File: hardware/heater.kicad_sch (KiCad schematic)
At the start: 5 parts

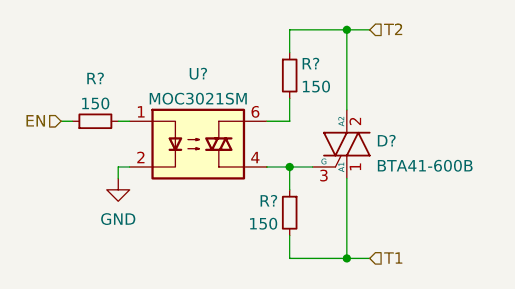
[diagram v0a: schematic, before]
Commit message: assigned footprints
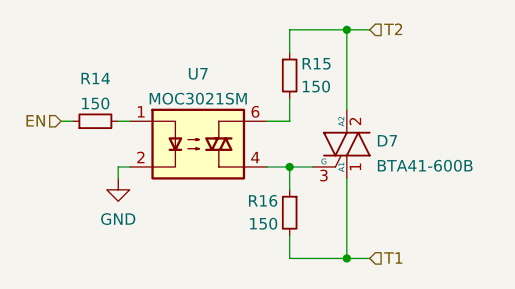
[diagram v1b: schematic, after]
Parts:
- D7: renamed from D?; footprint (none) -> Package_TO_SOT_THT:TO-3P-3_Horizontal_TabDown
- R14, R15, R16: renamed from R?; footprint (none) -> Resistor_SMD:R_0603_1608Metric
- gave numbers to parts that had none: 1
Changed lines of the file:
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@@
   (symbol (lib_id "Device:R_Small") (at 154.94 100.33 0)
     (in_bom yes) (on_board yes)
-    (property "Reference" "R?" (id 0) (at 156.21 99.06 0)
+    (property "Reference" "R15" (id 0) (at 156.21 99.06 0)
       (effects (font (size 1.27 1.27)) (justify left))
     )
@@
       (effects (font (size 1.27 1.27)) (justify left))
     )
-    (property "Footprint" "" (id 2) (at 154.94 100.33 0)
+    (property "Footprint" "Resistor_SMD:R_0603_1608Metric" (id 2) (at 154.94 100.33 0)
       (effects (font (size 1.27 1.27)) hide)
     )
@@
   (symbol (lib_id "power:GND") (at 135.89 111.76 0)
     (in_bom yes) (on_board yes) (fields_autoplaced)
-    (property "Reference" "#PWR?" (id 0) (at 135.89 118.11 0)
+    (property "Reference" "#PWR036" (id 0) (at 135.89 118.11 0)
       (effects (font (size 1.27 1.27)) hide)
     )
@@
   (symbol (lib_id "Isolator:TLP3021") (at 144.78 107.95 0)
     (in_bom yes) (on_board yes) (fields_autoplaced)
-    (property "Reference" "U?" (id 0) (at 144.78 100.1735 0))
+    (property "Reference" "U7" (id 0) (at 144.78 100.1735 0))
     (property "Value" "MOC3021SM" (id 1) (at 144.78 102.9486 0))
     (property "Footprint" "Package_DIP:SMDIP-6_W9.53mm_Clearance8mm" (id 2) (at 139.7 113.03 0)
@@
   (symbol (lib_id "Device:R_Small") (at 154.94 115.57 0) (mirror y)
     (in_bom yes) (on_board yes)
-    (property "Reference" "R?" (id 0) (at 153.67 114.3 0)
+    (property "Reference" "R16" (id 0) (at 153.67 114.3 0)
       (effects (font (size 1.27 1.27)) (justify left))
     )
@@
       (effects (font (size 1.27 1.27)) (justify left))
     )
-    (property "Footprint" "" (id 2) (at 154.94 115.57 0)
+    (property "Footprint" "Resistor_SMD:R_0603_1608Metric" (id 2) (at 154.94 115.57 0)
       (effects (font (size 1.27 1.27)) hide)
     )
@@
   (symbol (lib_id "Device:R_Small") (at 133.35 105.41 90)
     (in_bom yes) (on_board yes)
-    (property "Reference" "R?" (id 0) (at 133.35 100.7069 90))
+    (property "Reference" "R14" (id 0) (at 133.35 100.7069 90))
     (property "Value" "150" (id 1) (at 133.35 103.482 90))
-    (property "Footprint" "" (id 2) (at 133.35 105.41 0)
+    (property "Footprint" "Resistor_SMD:R_0603_1608Metric" (id 2) (at 133.35 105.41 0)
       (effects (font (size 1.27 1.27)) hide)
     )
@@
   (symbol (lib_id "Device:Q_TRIAC_A1A2G") (at 161.29 107.95 0)
     (in_bom yes) (on_board yes) (fields_autoplaced)
-    (property "Reference" "D?" (id 0) (at 164.5666 107.6257 0)
+    (property "Reference" "D7" (id 0) (at 164.5666 107.6257 0)
       (effects (font (size 1.27 1.27)) (justify left))
     )
@@
       (effects (font (size 1.27 1.27)) (justify left))
     )
-    (property "Footprint" "" (id 2) (at 163.195 107.315 90)
+    (property "Footprint" "Package_TO_SOT_THT:TO-3P-3_Horizontal_TabDown" (id 2) (at 163.195 107.315 90)
       (effects (font (size 1.27 1.27)) hide)
     )

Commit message: layout WIP
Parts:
- renumbered D7 to D6, R14 to R11, R15 to R12, R16 to R13, U7 to U6
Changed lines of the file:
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@@
   (symbol (lib_id "Device:R_Small") (at 154.94 100.33 0)
     (in_bom yes) (on_board yes)
-    (property "Reference" "R15" (id 0) (at 156.21 99.06 0)
+    (property "Reference" "R12" (id 0) (at 156.21 99.06 0)
       (effects (font (size 1.27 1.27)) (justify left))
     )
@@
   (symbol (lib_id "Isolator:TLP3021") (at 144.78 107.95 0)
     (in_bom yes) (on_board yes) (fields_autoplaced)
-    (property "Reference" "U7" (id 0) (at 144.78 100.1735 0))
+    (property "Reference" "U6" (id 0) (at 144.78 100.1735 0))
     (property "Value" "MOC3021SM" (id 1) (at 144.78 102.9486 0))
     (property "Footprint" "Package_DIP:SMDIP-6_W9.53mm_Clearance8mm" (id 2) (at 139.7 113.03 0)
@@
   (symbol (lib_id "Device:R_Small") (at 154.94 115.57 0) (mirror y)
     (in_bom yes) (on_board yes)
-    (property "Reference" "R16" (id 0) (at 153.67 114.3 0)
+    (property "Reference" "R13" (id 0) (at 153.67 114.3 0)
       (effects (font (size 1.27 1.27)) (justify left))
     )
@@
   (symbol (lib_id "Device:R_Small") (at 133.35 105.41 90)
     (in_bom yes) (on_board yes)
-    (property "Reference" "R14" (id 0) (at 133.35 100.7069 90))
+    (property "Reference" "R11" (id 0) (at 133.35 100.7069 90))
     (property "Value" "150" (id 1) (at 133.35 103.482 90))
     (property "Footprint" "Resistor_SMD:R_0603_1608Metric" (id 2) (at 133.35 105.41 0)
@@
   (symbol (lib_id "Device:Q_TRIAC_A1A2G") (at 161.29 107.95 0)
     (in_bom yes) (on_board yes) (fields_autoplaced)
-    (property "Reference" "D7" (id 0) (at 164.5666 107.6257 0)
+    (property "Reference" "D6" (id 0) (at 164.5666 107.6257 0)
       (effects (font (size 1.27 1.27)) (justify left))
     )

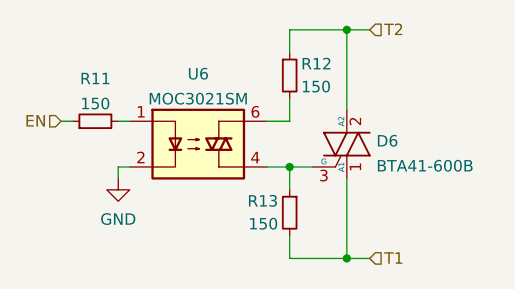
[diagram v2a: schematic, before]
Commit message: basic testing except heater done
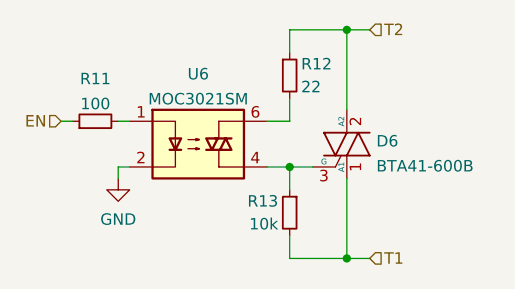
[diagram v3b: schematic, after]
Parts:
- R11: value 150 -> 100
- R12: value 150 -> 22
- R13: value 150 -> 10k
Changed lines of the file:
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@@
       (effects (font (size 1.27 1.27)) (justify left))
     )
-    (property "Value" "150" (id 1) (at 156.21 101.6 0)
+    (property "Value" "22" (id 1) (at 156.21 101.6 0)
       (effects (font (size 1.27 1.27)) (justify left))
     )
@@
   (symbol (lib_id "power:GND") (at 135.89 111.76 0)
     (in_bom yes) (on_board yes) (fields_autoplaced)
-    (property "Reference" "#PWR036" (id 0) (at 135.89 118.11 0)
+    (property "Reference" "#PWR035" (id 0) (at 135.89 118.11 0)
       (effects (font (size 1.27 1.27)) hide)
     )
@@
       (effects (font (size 1.27 1.27)) (justify left))
     )
-    (property "Value" "150" (id 1) (at 153.67 116.84 0)
+    (property "Value" "10k" (id 1) (at 153.67 116.84 0)
       (effects (font (size 1.27 1.27)) (justify left))
     )
@@
     (in_bom yes) (on_board yes)
     (property "Reference" "R11" (id 0) (at 133.35 100.7069 90))
-    (property "Value" "150" (id 1) (at 133.35 103.482 90))
+    (property "Value" "100" (id 1) (at 133.35 103.482 90))
     (property "Footprint" "Resistor_SMD:R_0603_1608Metric" (id 2) (at 133.35 105.41 0)
       (effects (font (size 1.27 1.27)) hide)

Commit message: added bang-bang implementation
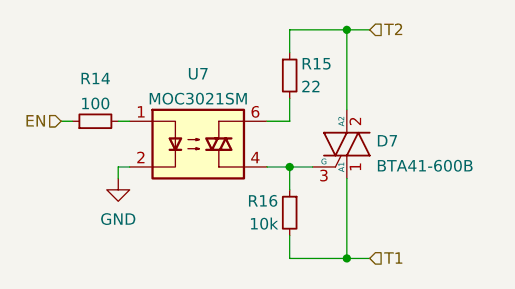
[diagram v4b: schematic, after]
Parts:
- renumbered D6 to D7, R11 to R14, R12 to R15, R13 to R16, U6 to U7
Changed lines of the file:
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@@
   (symbol (lib_id "Device:R_Small") (at 154.94 100.33 0)
     (in_bom yes) (on_board yes)
-    (property "Reference" "R12" (id 0) (at 156.21 99.06 0)
+    (property "Reference" "R15" (id 0) (at 156.21 99.06 0)
       (effects (font (size 1.27 1.27)) (justify left))
     )
@@
   (symbol (lib_id "power:GND") (at 135.89 111.76 0)
     (in_bom yes) (on_board yes) (fields_autoplaced)
-    (property "Reference" "#PWR035" (id 0) (at 135.89 118.11 0)
+    (property "Reference" "#PWR036" (id 0) (at 135.89 118.11 0)
       (effects (font (size 1.27 1.27)) hide)
     )
@@
   (symbol (lib_id "Isolator:TLP3021") (at 144.78 107.95 0)
     (in_bom yes) (on_board yes) (fields_autoplaced)
-    (property "Reference" "U6" (id 0) (at 144.78 100.1735 0))
+    (property "Reference" "U7" (id 0) (at 144.78 100.1735 0))
     (property "Value" "MOC3021SM" (id 1) (at 144.78 102.9486 0))
     (property "Footprint" "Package_DIP:SMDIP-6_W9.53mm_Clearance8mm" (id 2) (at 139.7 113.03 0)
@@
   (symbol (lib_id "Device:R_Small") (at 154.94 115.57 0) (mirror y)
     (in_bom yes) (on_board yes)
-    (property "Reference" "R13" (id 0) (at 153.67 114.3 0)
+    (property "Reference" "R16" (id 0) (at 153.67 114.3 0)
       (effects (font (size 1.27 1.27)) (justify left))
     )
@@
   (symbol (lib_id "Device:R_Small") (at 133.35 105.41 90)
     (in_bom yes) (on_board yes)
-    (property "Reference" "R11" (id 0) (at 133.35 100.7069 90))
+    (property "Reference" "R14" (id 0) (at 133.35 100.7069 90))
     (property "Value" "100" (id 1) (at 133.35 103.482 90))
     (property "Footprint" "Resistor_SMD:R_0603_1608Metric" (id 2) (at 133.35 105.41 0)
@@
   (symbol (lib_id "Device:Q_TRIAC_A1A2G") (at 161.29 107.95 0)
     (in_bom yes) (on_board yes) (fields_autoplaced)
-    (property "Reference" "D6" (id 0) (at 164.5666 107.6257 0)
+    (property "Reference" "D7" (id 0) (at 164.5666 107.6257 0)
       (effects (font (size 1.27 1.27)) (justify left))
     )

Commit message: update to KiCad 7
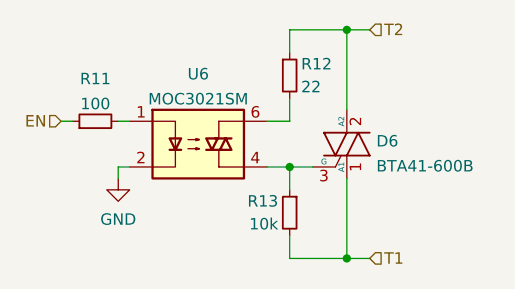
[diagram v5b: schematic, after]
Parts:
- renumbered D7 to D6, R14 to R11, R15 to R12, R16 to R13, U7 to U6
